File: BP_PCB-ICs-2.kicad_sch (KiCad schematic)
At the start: 8 parts, among them IC1 LMT84DCKT, U3 SN74CB3Q3257DBQR, U5 SN74CB3Q3257DBQR

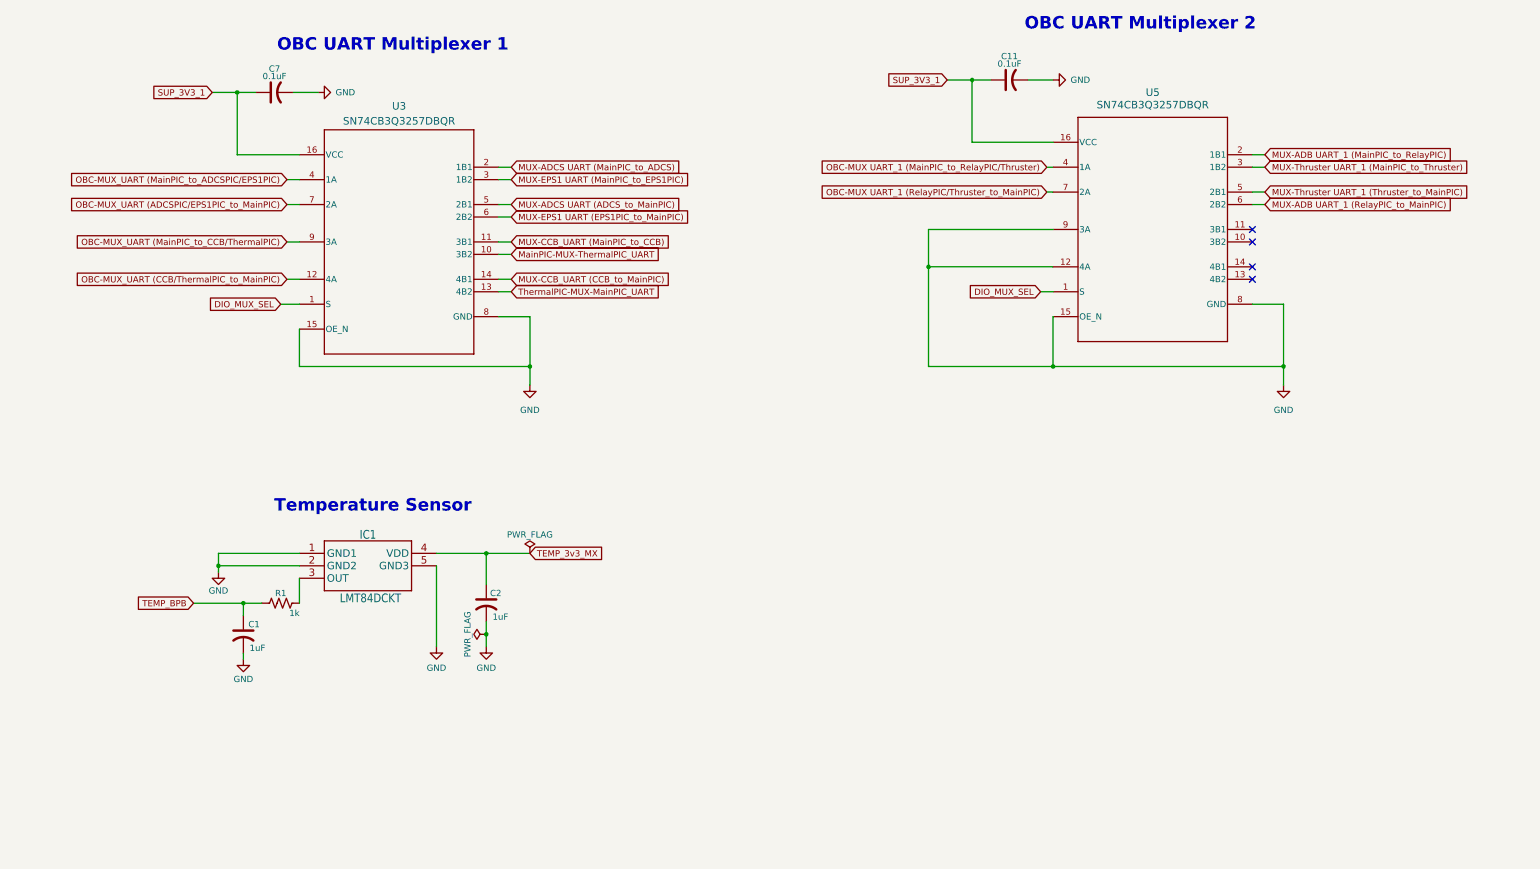
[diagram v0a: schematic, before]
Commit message: PCB layout is syncronized with schematic
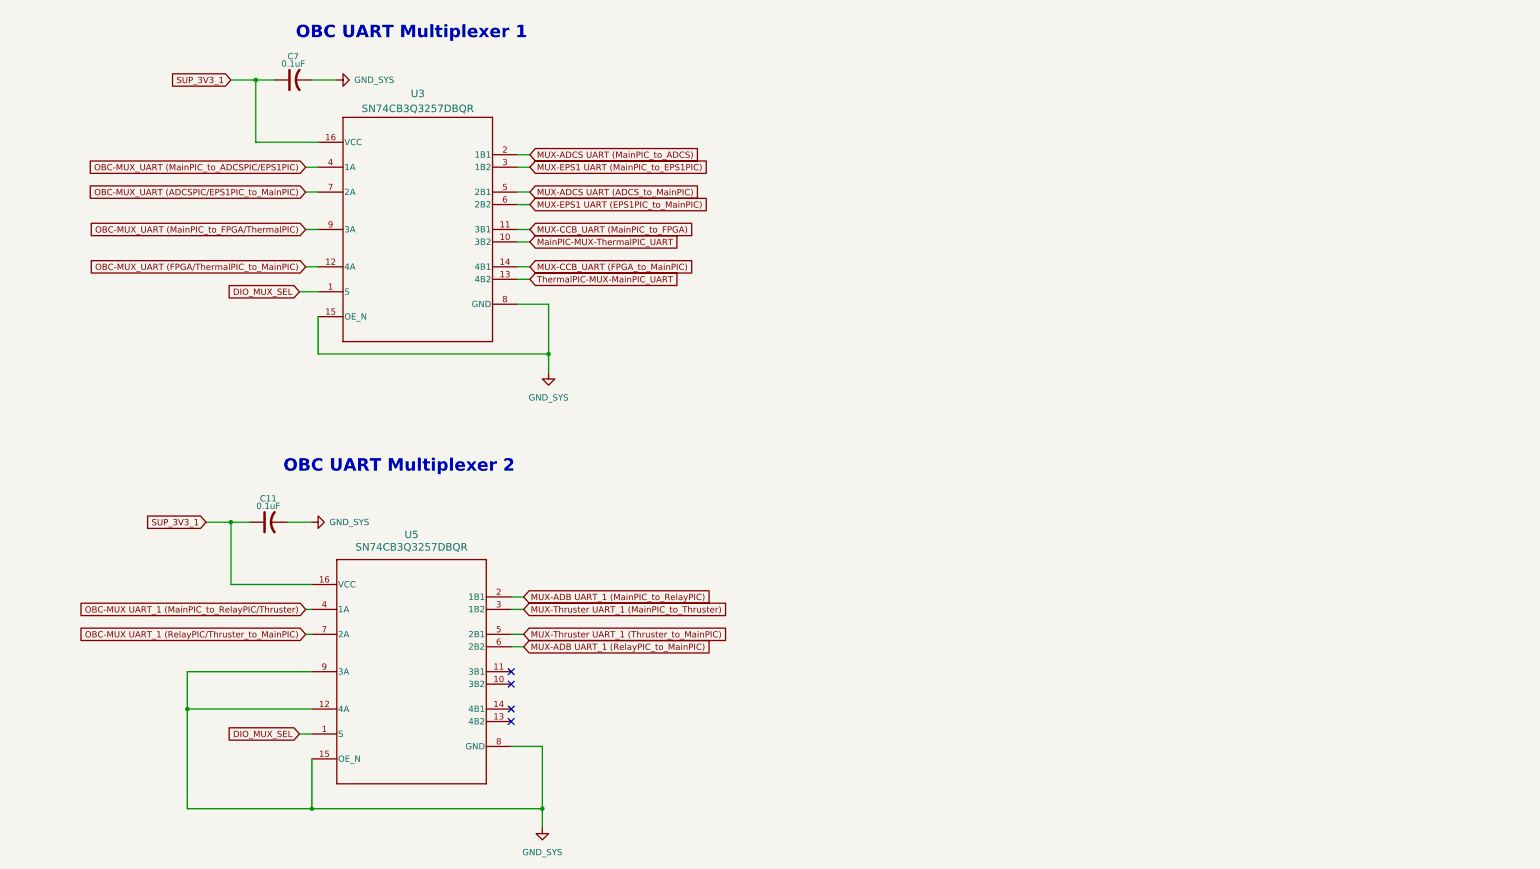
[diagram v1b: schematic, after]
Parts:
- removed C1, C2: 1uF, Capacitor_SMD:C_0805_2012Metric, symbol Device:C_US
- removed IC1: LMT84DCKT, Custom-Footprints:LMT84DCKT, symbol Custom-Symbols:LMT84DCKT
- removed R1: 1k, Resistor_SMD:R_0805_2012Metric, symbol Device:R_US
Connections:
- net GND renamed GND_SYS
- net MUX-CCB_UART (CCB_to_MainPIC) renamed MUX-CCB_UART (FPGA_to_MainPIC)
- net MUX-CCB_UART (MainPIC_to_CCB) renamed MUX-CCB_UART (MainPIC_to_FPGA)
- net OBC-MUX_UART (CCB/ThermalPIC_to_MainPIC) renamed OBC-MUX_UART (FPGA/ThermalPIC_to_MainPIC)
- net OBC-MUX_UART (MainPIC_to_CCB/ThermalPIC) renamed OBC-MUX_UART (MainPIC_to_FPGA/ThermalPIC)
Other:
- note removed: "Temperature Sensor"
- title: (none) -> BP PCB Ics-1
- moved on the sheet: C11, C7, U3, U5

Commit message: Finished routing and NO DRC errors
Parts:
- C11, C7: LCSC Part (none) -> C1711
- U3, U5: LCSC Part (none) -> C7138
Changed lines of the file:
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@@
+			)
+		)
+		(property "LCSC Part" "C1711"
+			(at 74.93 124.46 90)
+			(effects
+				(font
+					(size 1.27 1.27)
+				)
+				(hide yes)
 			)
 		)
@@
 		)
 		(property "Description" ""
+			(at 105.41 64.77 0)
+			(effects
+				(font
+					(size 1.27 1.27)
+				)
+				(hide yes)
+			)
+		)
+		(property "LCSC Part" "C7138"
 			(at 105.41 64.77 0)
 			(effects
@@
 			)
 		)
+		(property "LCSC Part" "C7138"
+			(at 104.14 154.94 0)
+			(effects
+				(font
+					(size 1.27 1.27)
+				)
+				(hide yes)
+			)
+		)
 		(pin "10"
 		)
@@
 			(effects
 				(font
+					(size 1.27 1.27)
+				)
+				(hide yes)
+			)
+		)
+		(property "LCSC Part" "C1711"
+			(at 80.01 34.29 90)
+			(effects
+				(font

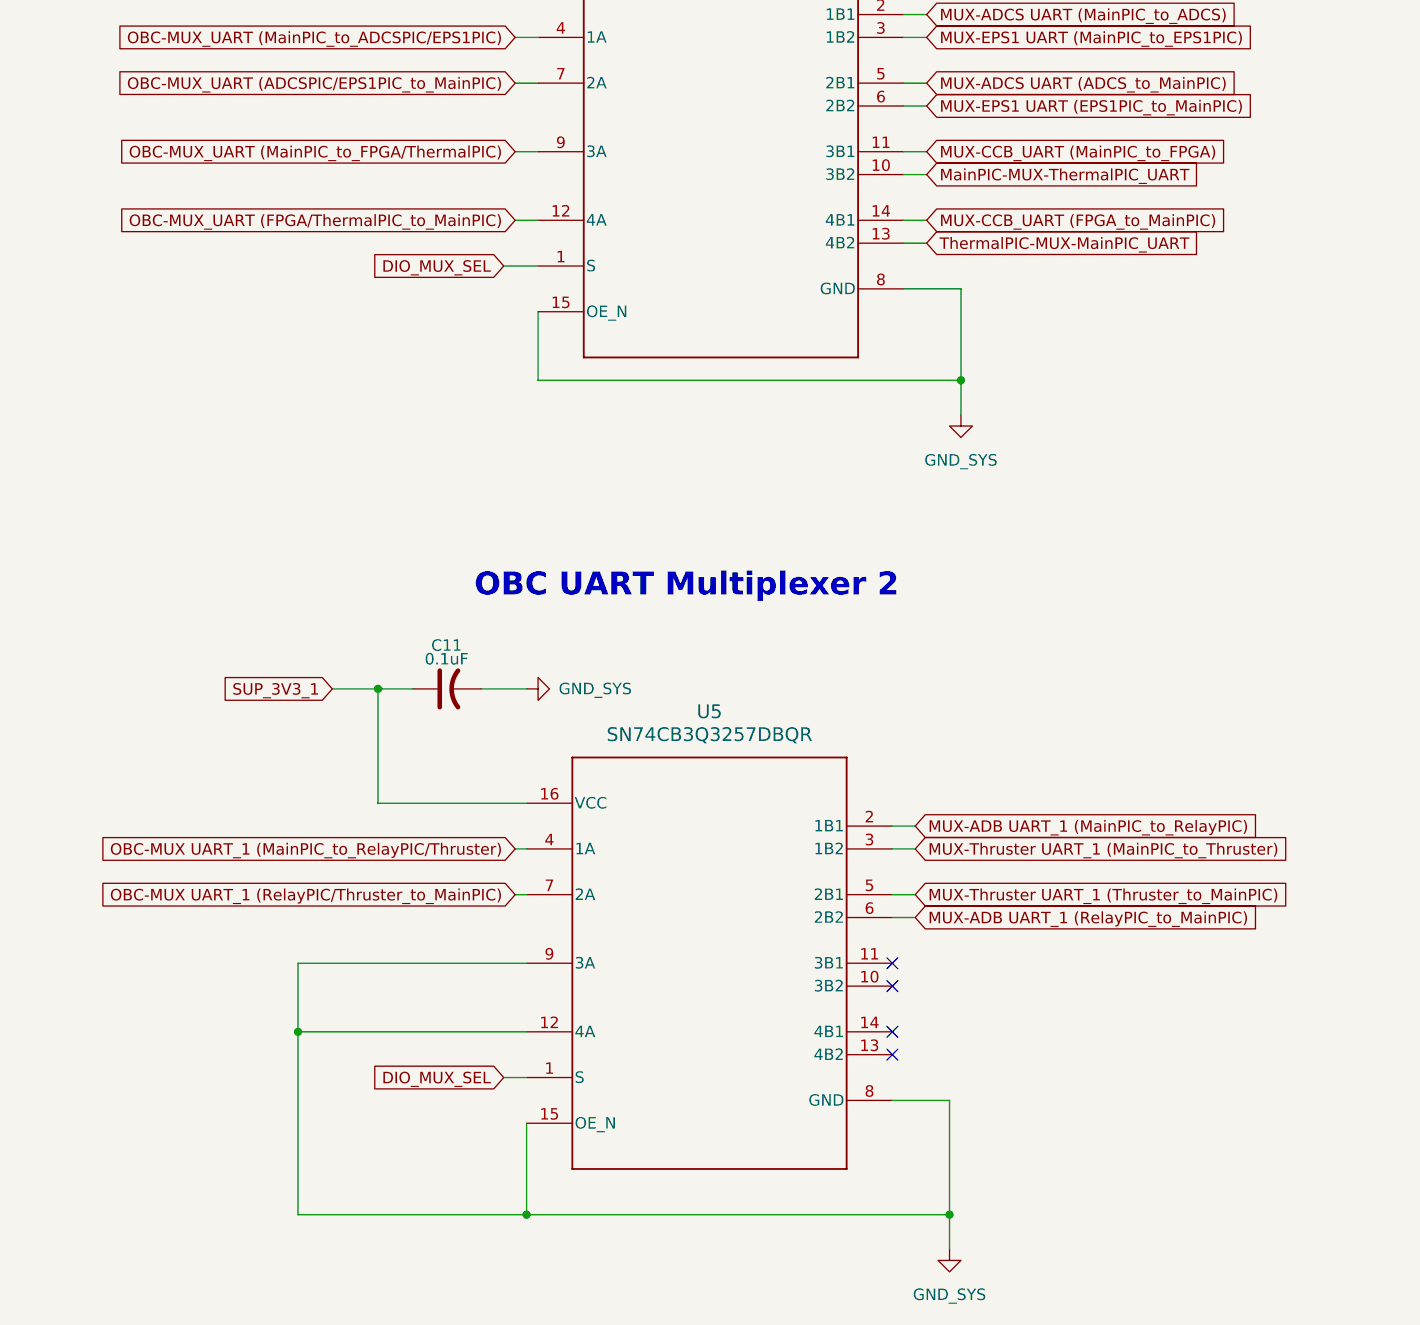
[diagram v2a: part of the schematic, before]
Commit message: Corrected OCP values in schematic and fixed PCB layout
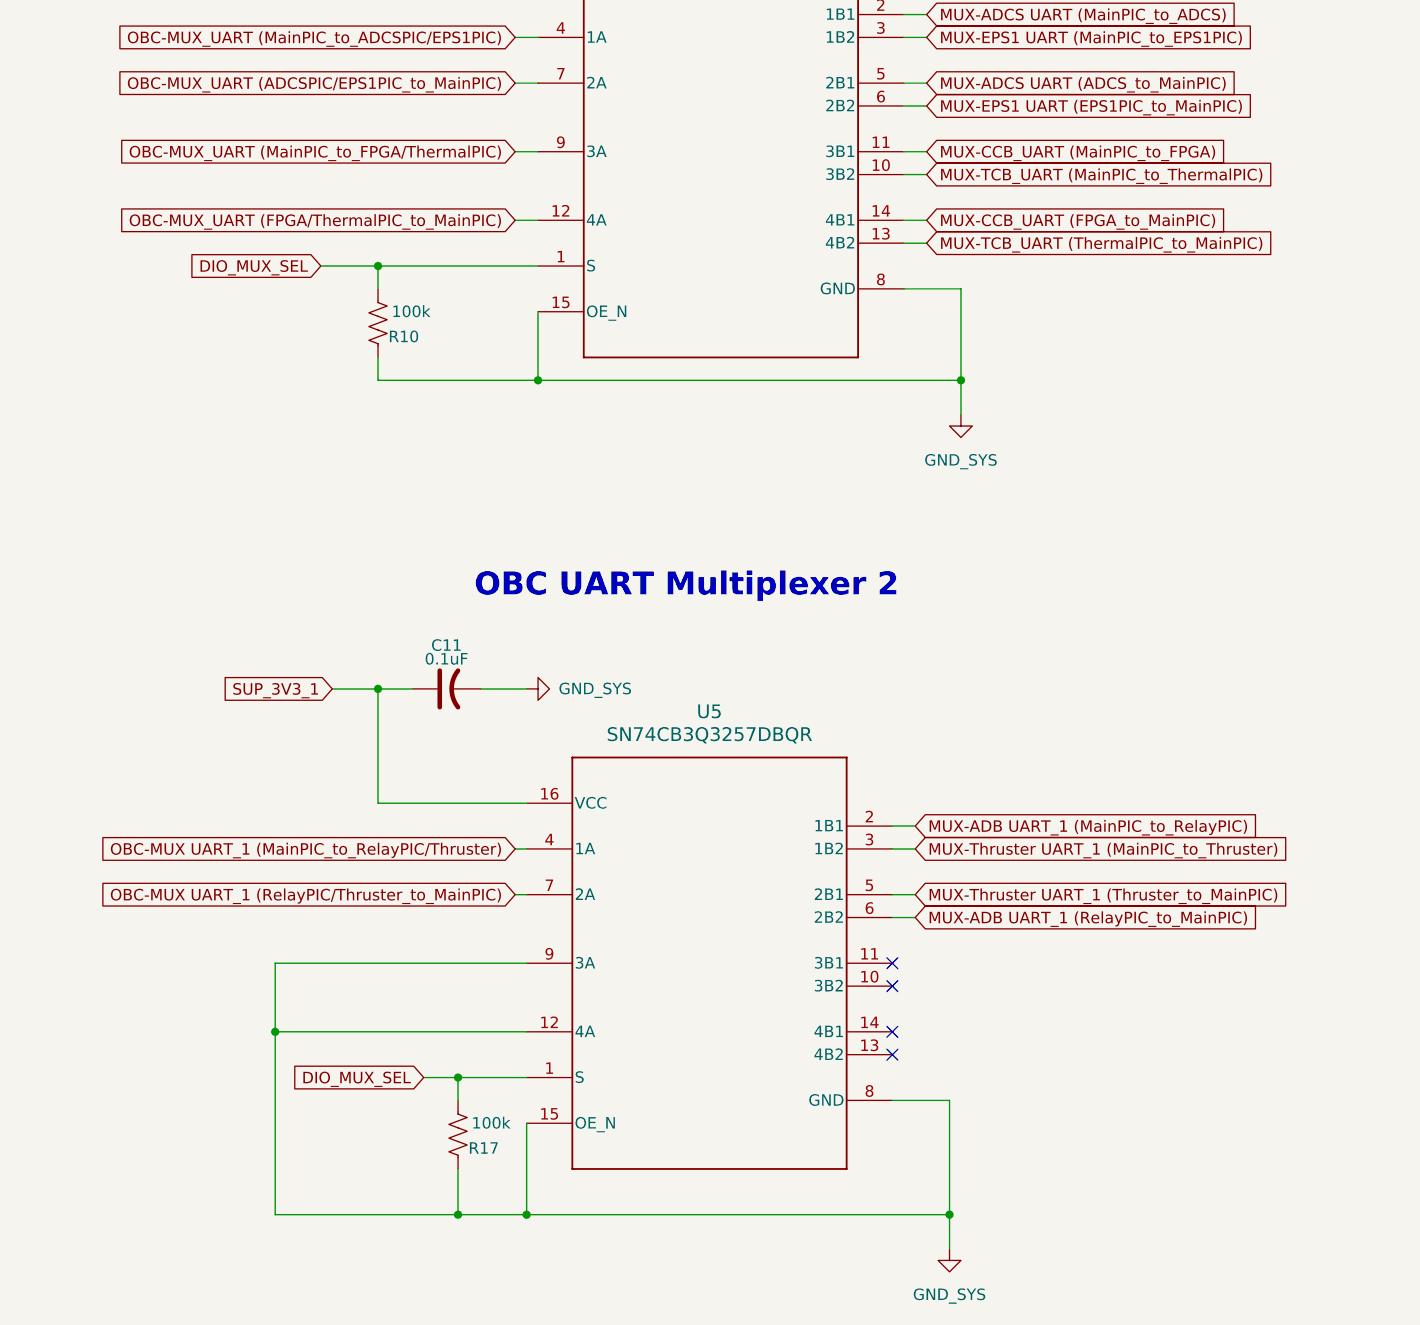
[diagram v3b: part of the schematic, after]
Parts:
- added R10, R17: 100k, Resistor_SMD:R_0805_2012Metric, symbol Device:R_US
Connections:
- net DIO_MUX_SEL: now also R10.2, R17.2
- net GND_SYS: now also R10.1, R17.1
- net MainPIC-MUX-ThermalPIC_UART renamed MUX-TCB_UART (MainPIC_to_ThermalPIC)
- net ThermalPIC-MUX-MainPIC_UART  renamed MUX-TCB_UART (ThermalPIC_to_MainPIC)

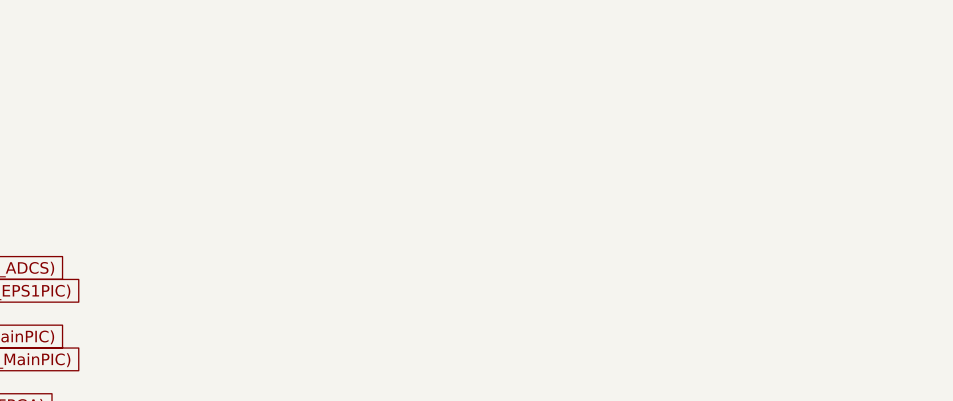
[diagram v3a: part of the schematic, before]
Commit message: Added grounded mounting holes to schematics
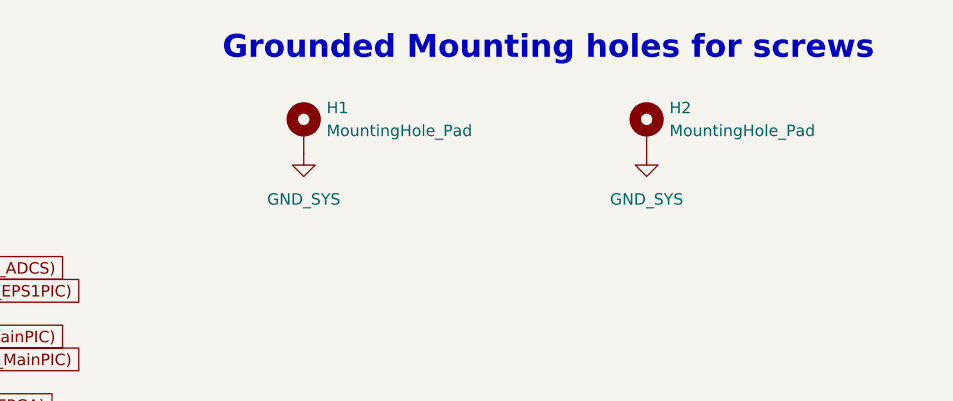
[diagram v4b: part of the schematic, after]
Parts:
- added H1, H2: MountingHole_Pad, MountingHole:MountingHole_2.7mm_Pad, symbol Mechanical:MountingHole_Pad
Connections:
- net GND_SYS: now also H1.1, H2.1
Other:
- note added: "Grounded Mounting holes for screws"
